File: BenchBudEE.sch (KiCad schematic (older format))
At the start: 0 parts

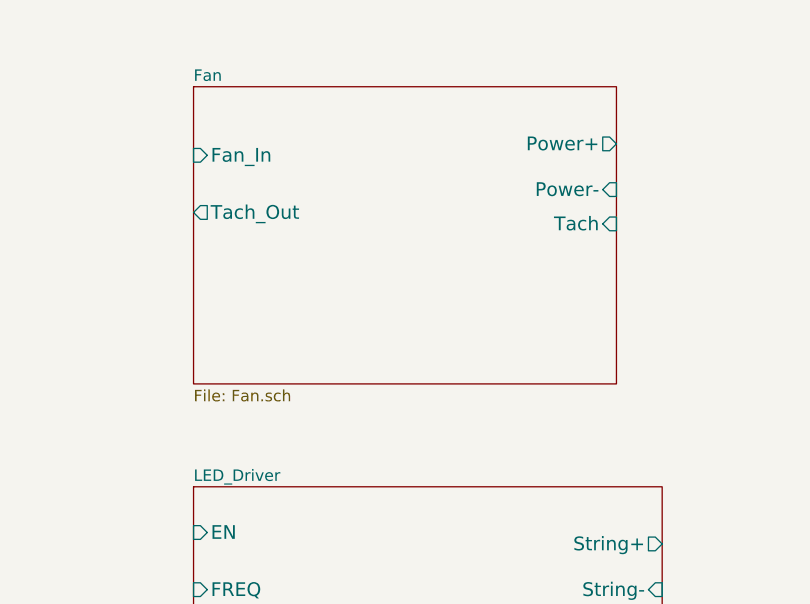
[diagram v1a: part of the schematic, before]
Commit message: Create Initial Fan Module Schematic
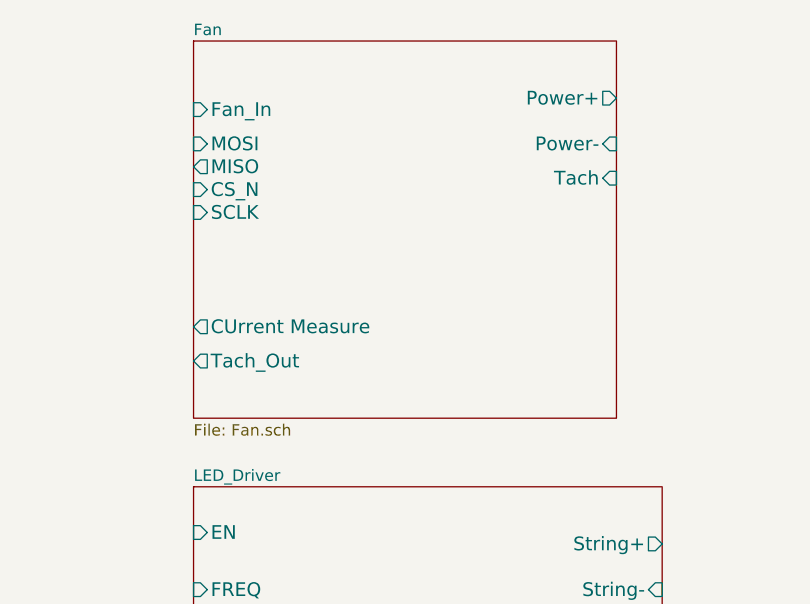
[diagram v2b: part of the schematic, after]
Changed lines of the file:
@@
 Sheet 1 8
 Title ""
-Date "4 feb 2014"
+Date "5 feb 2014"
 Rev ""
 Comp ""
@@
 $EndSheet
 $Sheet
-S 7400 1000 1850 1300
+S 7400 800  1850 1650
 U 52EECDEA
 F0 "Fan" 50
 F1 "Fan.sch" 50
-F2 "Power+" O R 9250 1250 60
-F3 "Power-" I R 9250 1450 60
-F4 "Tach" I R 9250 1600 60
-F5 "Tach_Out" O L 7400 1550 60
-F6 "Fan_In" I L 7400 1300 60
+F2 "Power+" O R 9250 1050 60
+F3 "Power-" I R 9250 1250 60
+F4 "Tach" I R 9250 1400 60
+F5 "Tach_Out" O L 7400 2200 60
+F6 "Fan_In" I L 7400 1100 60
+F7 "CUrrent Measure" O L 7400 2050 60
+F8 "MOSI" I L 7400 1250 60
+F9 "MISO" O L 7400 1350 60
+F10 "CS_N" I L 7400 1450 60
+F11 "SCLK" I L 7400 1550 60
 $EndSheet
 $Sheet

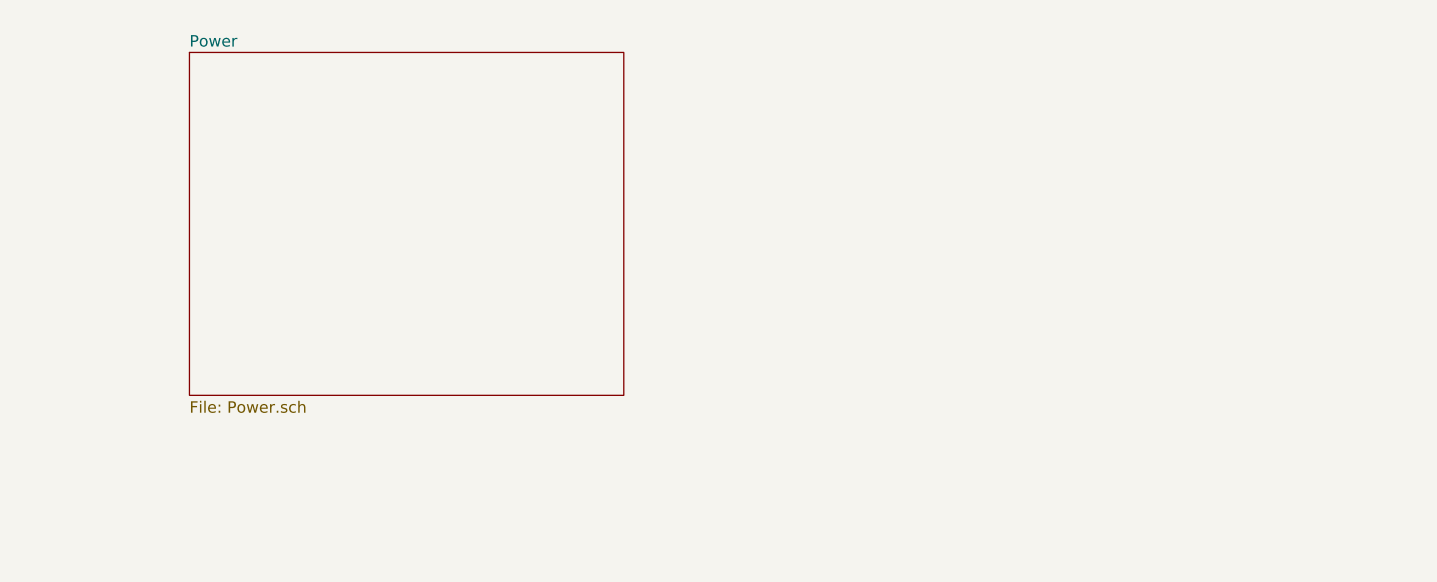
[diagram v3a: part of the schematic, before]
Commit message: Wire up Power Schematic
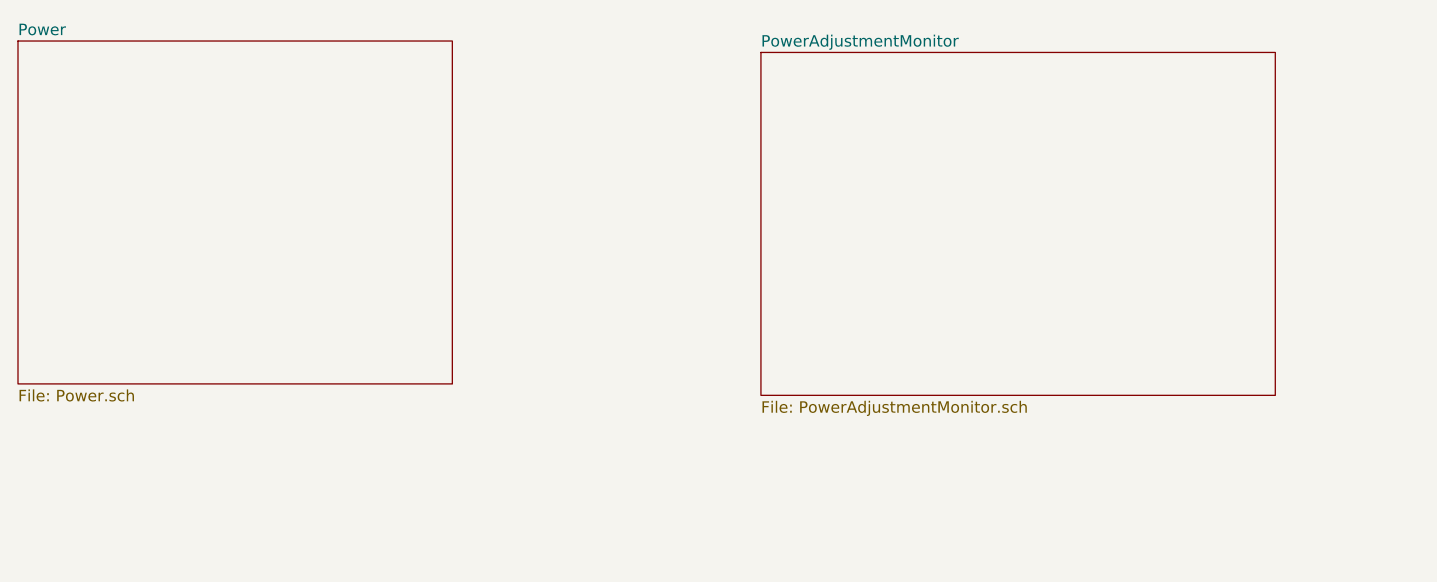
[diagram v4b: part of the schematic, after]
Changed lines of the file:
@@
 $Descr A4 11693 8268
 encoding utf-8
-Sheet 1 8
+Sheet 1 9
 Title ""
 Date "5 feb 2014"
@@
 $EndSheet
 $Sheet
-S 1500 800  1900 1500
+S 750  750  1900 1500
 U 52EECD90
 F0 "Power" 50
@@
 F7 "MOSI" I L 7400 4450 60
 $EndSheet
+$Sheet
+S 4000 800  2250 1500
+U 52F245F0
+F0 "PowerAdjustmentMonitor" 50
+F1 "PowerAdjustmentMonitor.sch" 50
+$EndSheet
 $EndSCHEMATC

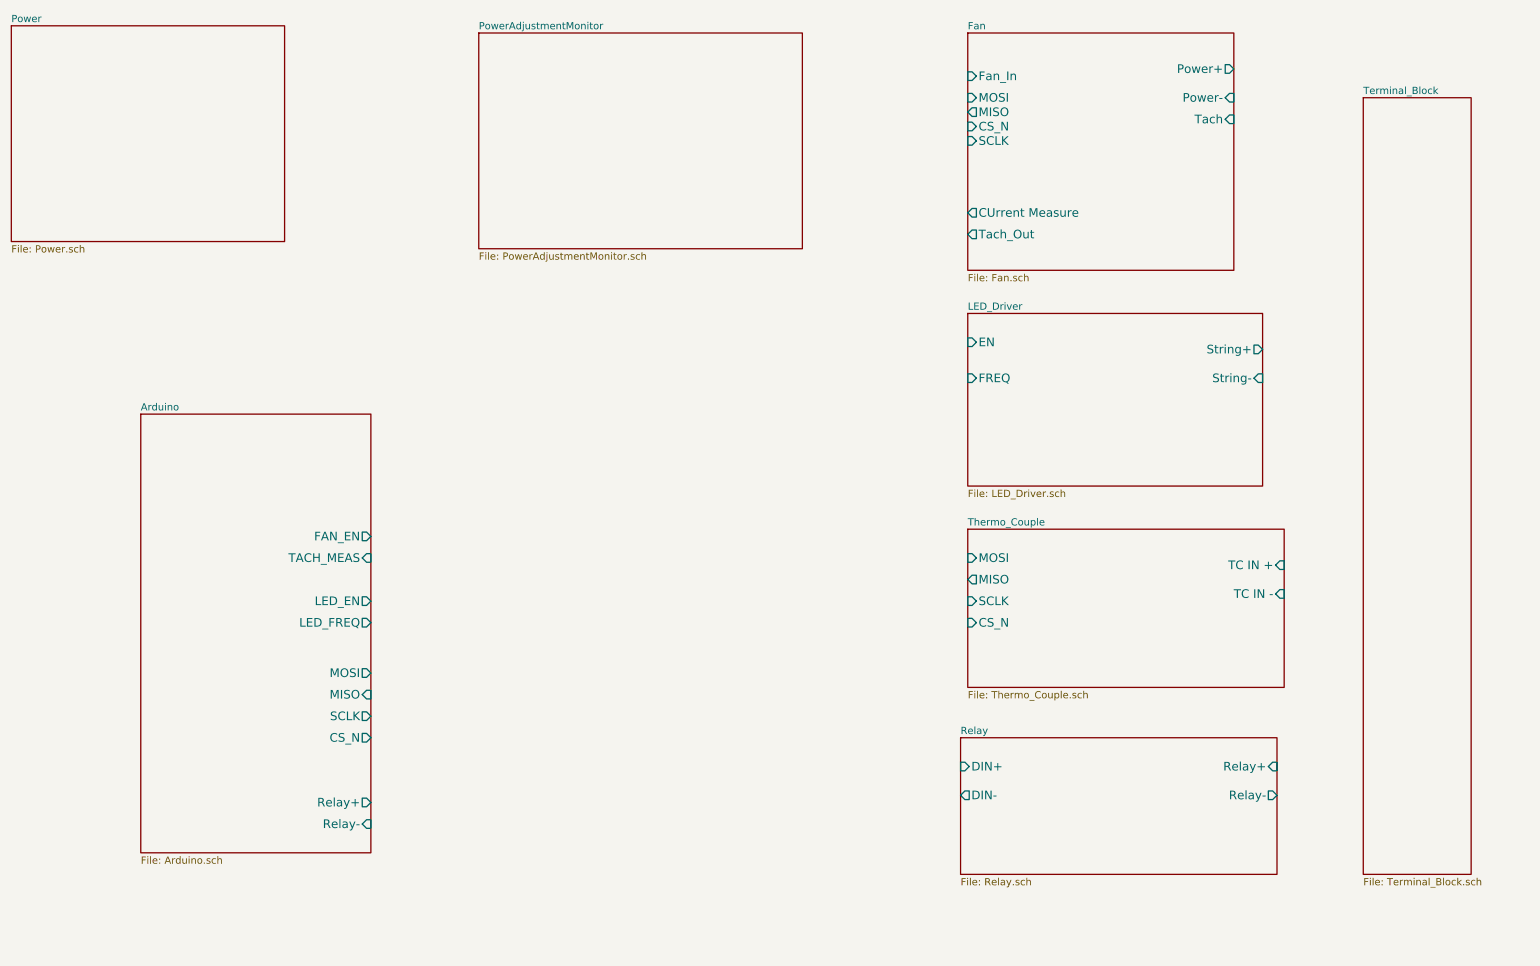
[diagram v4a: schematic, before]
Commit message: Added Power Control Monitoring Module Schematic
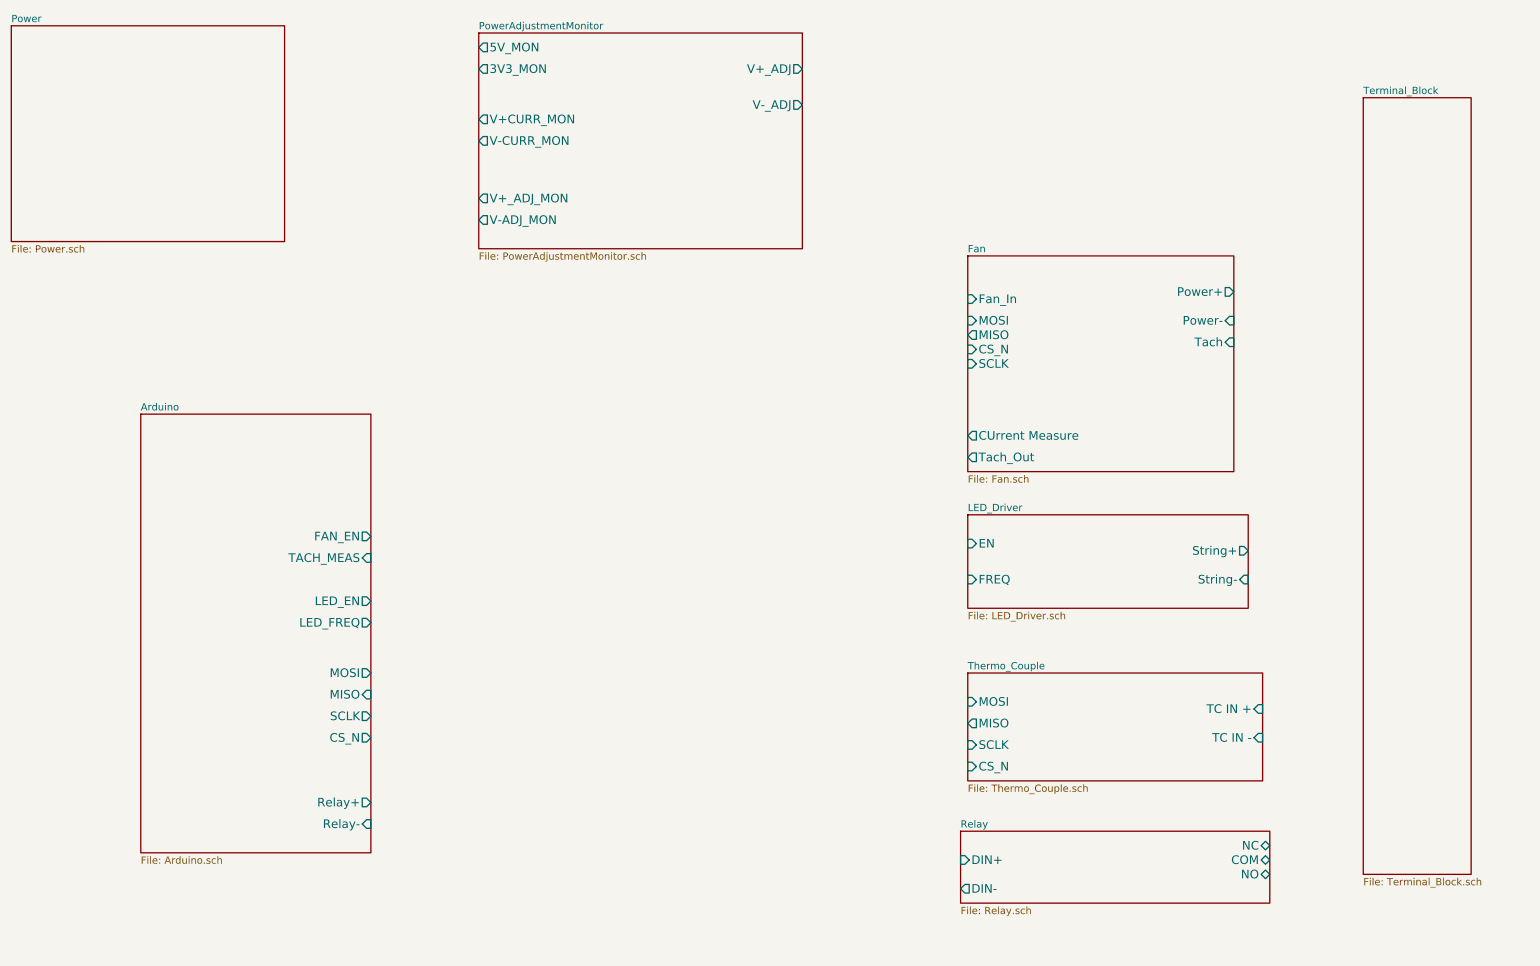
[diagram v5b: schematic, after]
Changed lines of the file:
@@
 $EndSheet
 $Sheet
-S 7350 5700 2200 950
+S 7350 6350 2150 500
 U 52EECD80
 F0 "Relay" 50
 F1 "Relay.sch" 50
-F2 "DIN+" I L 7350 5900 60
-F3 "DIN-" O L 7350 6100 60
-F4 "Relay+" I R 9550 5900 60
-F5 "Relay-" O R 9550 6100 60
+F2 "DIN+" I L 7350 6550 60
+F3 "DIN-" O L 7350 6750 60
+F4 "NC" B R 9500 6450 60
+F5 "NO" B R 9500 6650 60
+F6 "COM" B R 9500 6550 60
 $EndSheet
 $Sheet
@@
 $EndSheet
 $Sheet
-S 7400 2750 2050 1200
+S 7400 4150 1950 650
 U 52EECDCB
 F0 "LED_Driver" 50
 F1 "LED_Driver.sch" 50
-F2 "EN" I L 7400 2950 60
-F3 "FREQ" I L 7400 3200 60
-F4 "String+" O R 9450 3000 60
-F5 "String-" I R 9450 3200 60
+F2 "EN" I L 7400 4350 60
+F3 "FREQ" I L 7400 4600 60
+F4 "String+" O R 9350 4400 60
+F5 "String-" I R 9350 4600 60
 $EndSheet
 $Sheet
-S 7400 800  1850 1650
+S 7400 2350 1850 1500
 U 52EECDEA
 F0 "Fan" 50
 F1 "Fan.sch" 50
-F2 "Power+" O R 9250 1050 60
-F3 "Power-" I R 9250 1250 60
-F4 "Tach" I R 9250 1400 60
-F5 "Tach_Out" O L 7400 2200 60
-F6 "Fan_In" I L 7400 1100 60
-F7 "CUrrent Measure" O L 7400 2050 60
-F8 "MOSI" I L 7400 1250 60
-F9 "MISO" O L 7400 1350 60
-F10 "CS_N" I L 7400 1450 60
-F11 "SCLK" I L 7400 1550 60
+F2 "Power+" O R 9250 2600 60
+F3 "Power-" I R 9250 2800 60
+F4 "Tach" I R 9250 2950 60
+F5 "Tach_Out" O L 7400 3750 60
+F6 "Fan_In" I L 7400 2650 60
+F7 "CUrrent Measure" O L 7400 3600 60
+F8 "MOSI" I L 7400 2800 60
+F9 "MISO" O L 7400 2900 60
+F10 "CS_N" I L 7400 3000 60
+F11 "SCLK" I L 7400 3100 60
 $EndSheet
 $Sheet
@@
 $EndSheet
 $Sheet
-S 7400 4250 2200 1100
+S 7400 5250 2050 750
 U 52EECD62
 F0 "Thermo_Couple" 50
 F1 "Thermo_Couple.sch" 50
-F2 "TC IN +" I R 9600 4500 60
-F3 "TC IN -" I R 9600 4700 60
-F4 "MISO" O L 7400 4600 60
-F5 "SCLK" I L 7400 4750 60
-F6 "CS_N" I L 7400 4900 60
-F7 "MOSI" I L 7400 4450 60
+F2 "TC IN +" I R 9450 5500 60
+F3 "TC IN -" I R 9450 5700 60
+F4 "MISO" O L 7400 5600 60
+F5 "SCLK" I L 7400 5750 60
+F6 "CS_N" I L 7400 5900 60
+F7 "MOSI" I L 7400 5450 60
 $EndSheet
 $Sheet
@@
 F0 "PowerAdjustmentMonitor" 50
 F1 "PowerAdjustmentMonitor.sch" 50
+F2 "V+_ADJ" O R 6250 1050 60
+F3 "V-_ADJ" O R 6250 1300 60
+F4 "3V3_MON" O L 4000 1050 60
+F5 "5V_MON" O L 4000 900 60
+F6 "V+_ADJ_MON" O L 4000 1950 60
+F7 "V-ADJ_MON" O L 4000 2100 60
+F8 "V+CURR_MON" O L 4000 1400 60
+F9 "V-CURR_MON" O L 4000 1550 60
 $EndSheet
 $EndSCHEMATC
